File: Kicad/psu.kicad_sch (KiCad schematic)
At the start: 19 parts, among them J14 Conn_01x03_Pin, J15 Conn_01x03_Pin, J16 Conn_01x03_Pin, U15 L7912, U2 L7812, U3 XL1509-5.0

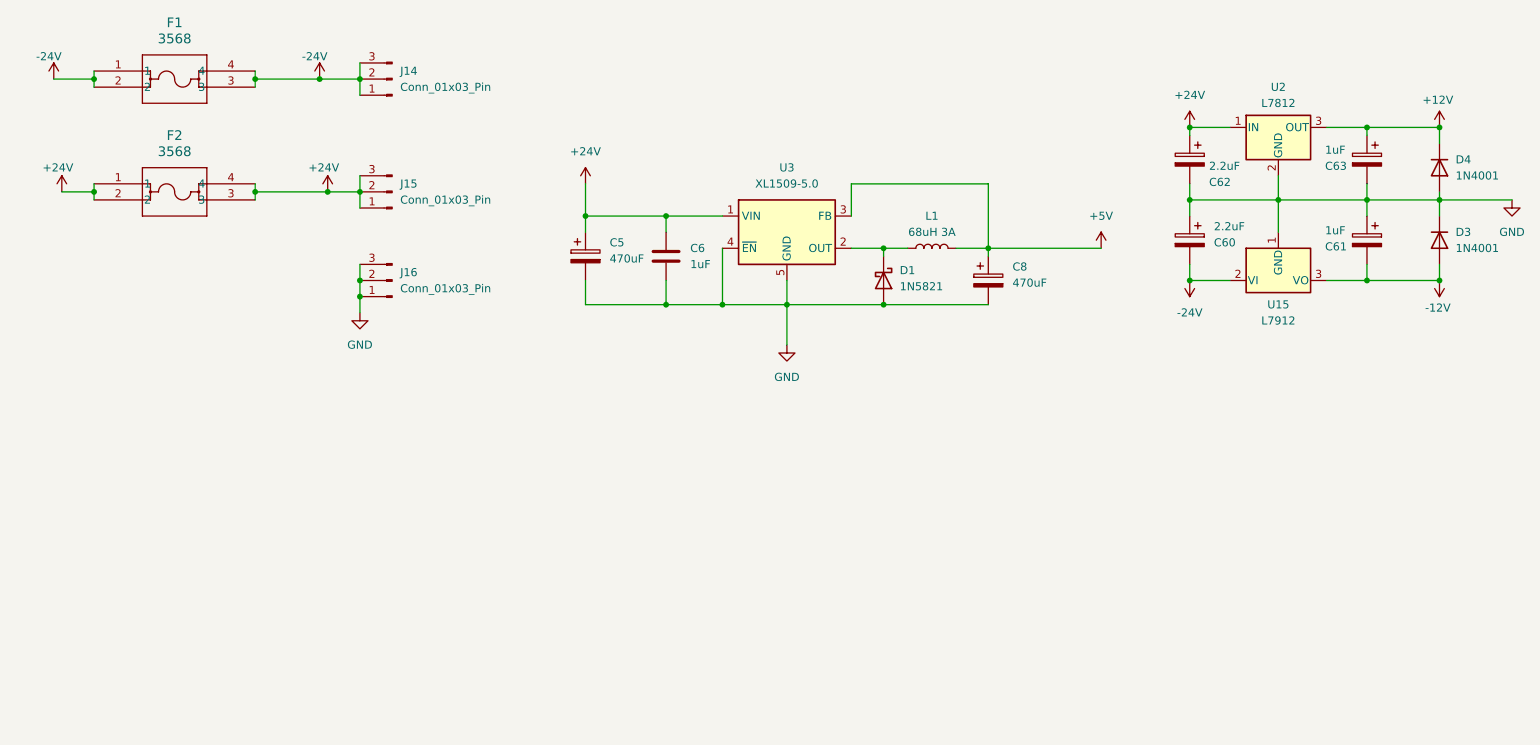
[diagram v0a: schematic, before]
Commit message: moved dac to input path and added input multiplexing
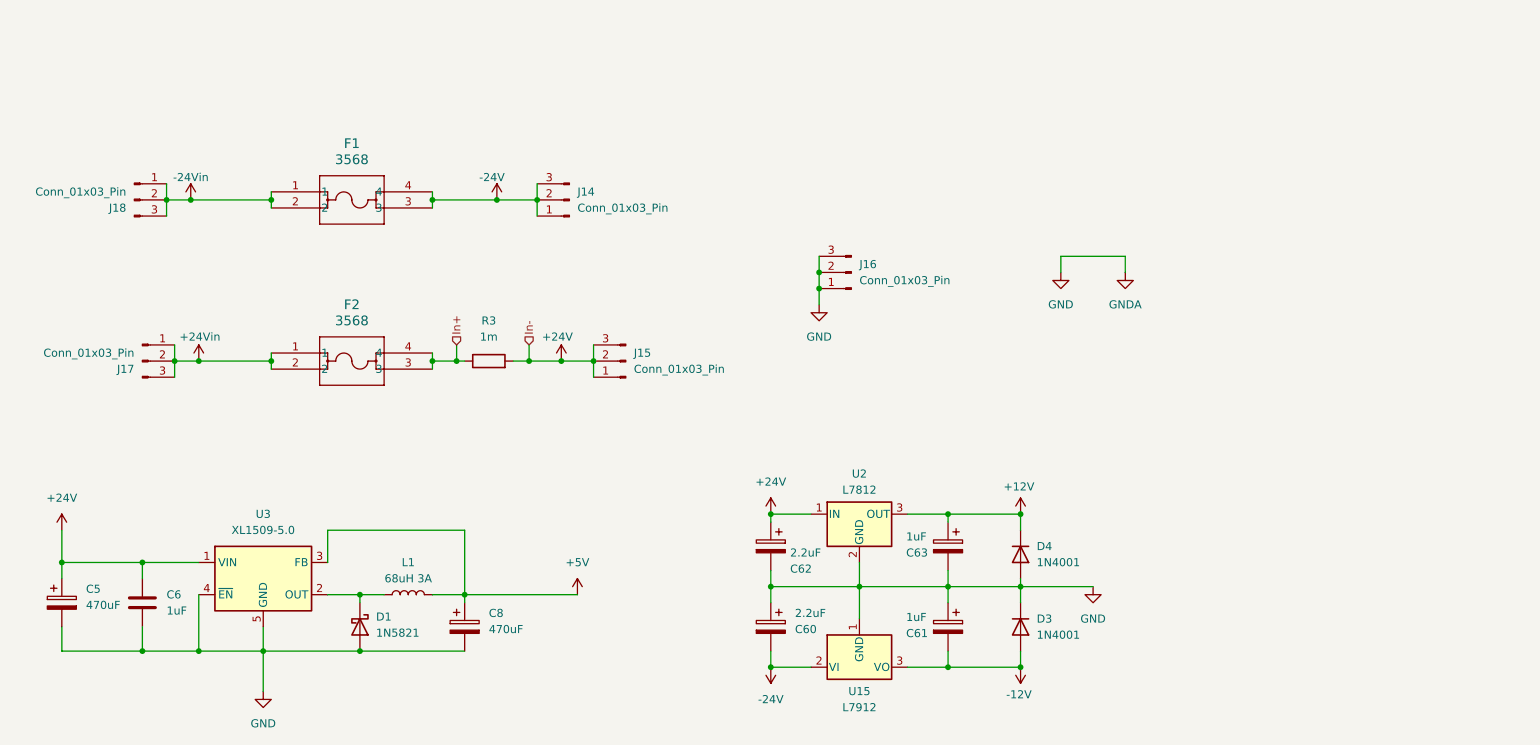
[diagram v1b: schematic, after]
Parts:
- added J17, J18: Conn_01x03_Pin, symbol Connector:Conn_01x03_Pin
- added R3: 1m, symbol Device:R
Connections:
- net +24V: now also R3.2; no longer F2.1, F2.2, F2.3, F2.4
- net -24V: no longer F1.1, F1.2
- new net +24Vin: F2.1, F2.2, J17.1 (Pin_1), J17.2 (Pin_2), J17.3 (Pin_3)
- new net -24Vin: F1.1, F1.2, J18.1 (Pin_1), J18.2 (Pin_2), J18.3 (Pin_3)
- new net In+: F2.3, F2.4, R3.1
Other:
- moved on the sheet: C5, C6, C60, C61, C62, C63, C8, D1, D3, D4, F1, F2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

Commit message: final schematic
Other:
- moved on the sheet: C5, C6, C60, C61, C62, C63, C8, D1, D3, D4, J16, L1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
